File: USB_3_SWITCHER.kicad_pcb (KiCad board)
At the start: 4 copper layers, 122 x 56 mm, 218 parts, among them J1 Jack-DC, J2 Wuerth_USB3_B_Receptable_6922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, J3 Wuerth_USB3_B_Receptable_6922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, J4 Wuerth_USB3_Receptible_692122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, J5 Wuerth_USB3_Receptible_692122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, J6 Wuerth_USB3_Receptible_692122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, J7 Wuerth_USB3_Receptible_692122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, J8 Conn_01x16_Pin, J9 Conn_01x04_Pin, Q1 NTJD4401NT1G, Q2 NTJD4401NT1G, SW1 SW_Omron_B3FS, U1 AT24CS04-SSHM, U10 LM66100DCK, U11 TPD6E05U06RVZ, U12 MAX8586, U13 TPD6E05U06RVZ, U14 MAX8586, U15 TPD6E05U06RVZ, U16 MAX8586, U17 TPD6E05U06RVZ, U18 MAX8586, U19 TPD6E05U06RVZ, U2 TUSB8043A, U20 74LVC1G08, U21 74LVC1G08, U22 LM397, U3 TS3USB30EDGSR, U4 CBTL02043A, U5 LM66100DCK, U6 LMR33640ADDA, U7 LMR33640ADDA, U8 LM66100DCK, U9 TPD6E05U06RVZ, Y1 24MHz 20ppm

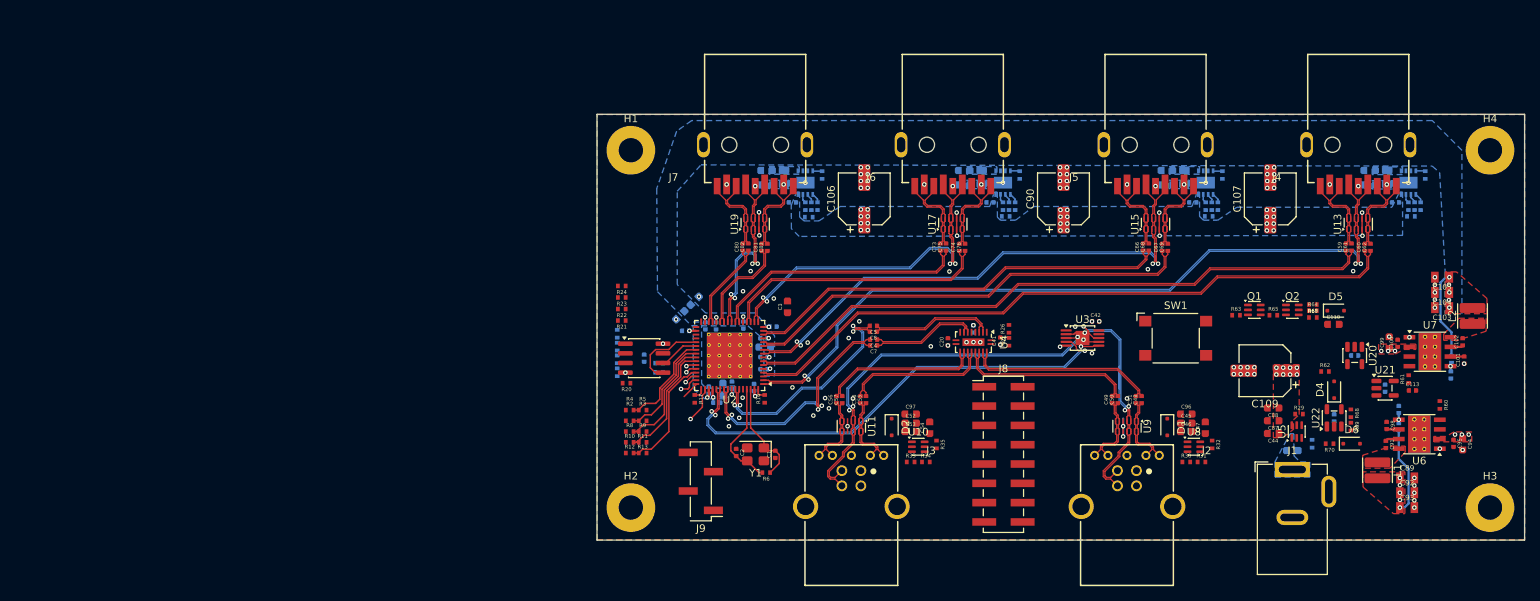
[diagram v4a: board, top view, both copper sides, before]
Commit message: Button & Power Sequencing + Layout
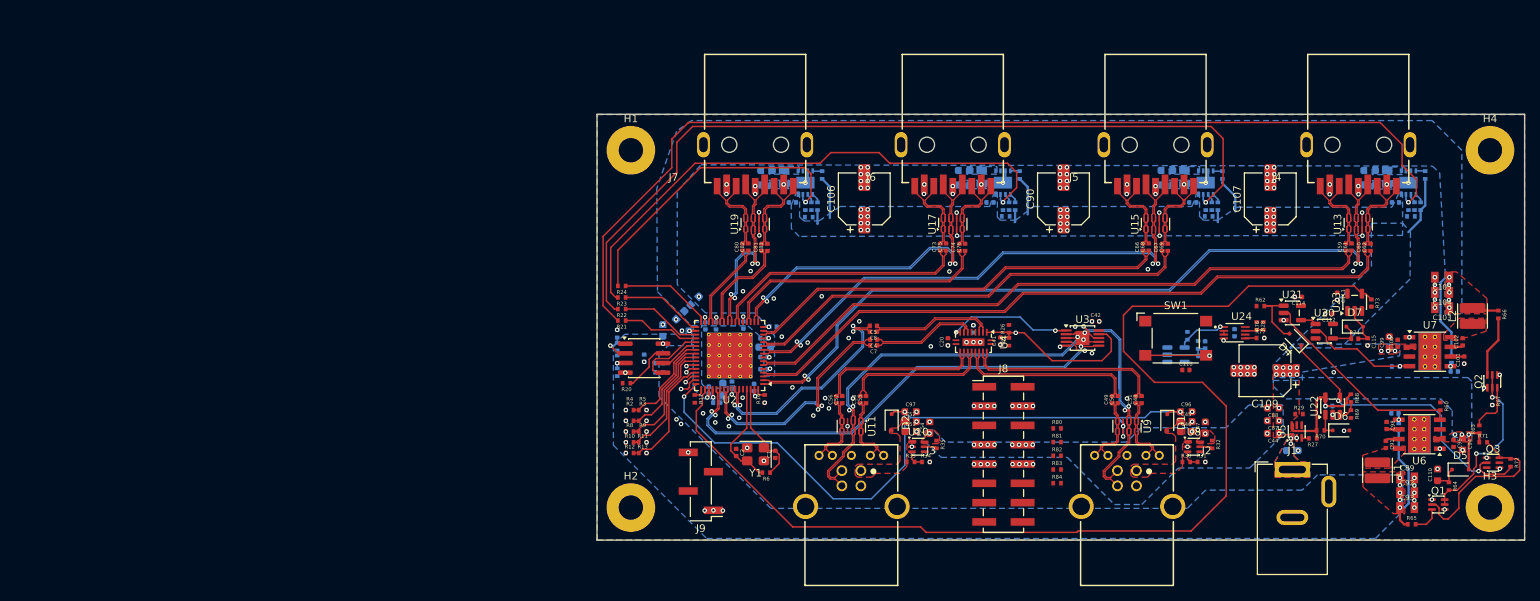
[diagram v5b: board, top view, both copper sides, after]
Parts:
- added C115: 1u, 00_Capacitor:Cap_0402, F.Cu at (242.3, 132.4)
- added C116: 100n, 00_Capacitor:Cap_0402, B.Cu at (224.8, 131.2)
- added C117: 1u, 00_Capacitor:Cap_0402, B.Cu at (221.0, 132.8)
- added C118: 100n, 00_Capacitor:Cap_0402, F.Cu at (218.4, 136.1)
- added D7: BAT54J, Diode_SMD:D_SOD-323F, F.Cu at (240.7, 130.4)
- added Q3: NTJD4401NT1G, Package_TO_SOT_SMD:SOT-363_SC-70-6, F.Cu at (258.9, 148.3)
- added R28: 10k, 00_Resistor:Res_0402, F.Cu at (227.8, 130.3)
- added R71: 1k, 00_Resistor:Res_0402, F.Cu at (257.6, 145.6)
- added R72: 0, 00_Resistor:Res_0402, F.Cu at (261.1, 148.3)
- added R73: 1K, 00_Capacitor:Cap_0402, F.Cu at (242.8, 127.3)
- added R74: 1K, 00_Capacitor:Cap_0402, F.Cu at (240.7, 132.0)
- added R75: 1K, 00_Capacitor:Cap_0402, B.Cu at (220.5, 134.3)
- added R76: 10k, 00_Resistor:Res_0402, F.Cu at (228.7, 130.3)
- added R77: 10k, 00_Resistor:Res_0402, F.Cu at (228.2, 131.9)
- added R78: 10k, 00_Resistor:Res_0402, B.Cu at (218.7, 131.6)
- added R79: 10k, 00_Resistor:Res_0402, B.Cu at (220.1, 132.8)
- added R80: 0, 00_Resistor:Res_0402, F.Cu at (201.5, 143.8)
- added R81: 0, 00_Resistor:Res_0402, F.Cu at (201.5, 145.6)
- added R82: 0, 00_Resistor:Res_0402, F.Cu at (201.5, 147.4)
- added R83: 0, 00_Resistor:Res_0402, F.Cu at (201.5, 149.2)
- added R84: 0, 00_Resistor:Res_0402, F.Cu at (201.5, 151.0)
- added U23: 74LVC1G17, Package_TO_SOT_SMD:SOT-23-5, F.Cu at (240.7, 127.2)
- added U24: 74LVC2G74, 00_IC_Package_Misc:SOP50P310X90-8N, F.Cu at (224.8, 131.2)
- added U25: 74LVC1G17, Package_TO_SOT_SMD:SOT-23-5, B.Cu at (217.2, 134.1)
- C112, C114, R27: moved to F.Cu
- C3, R61: moved to B.Cu
- R64, R70: value 10k -> 1k
- moved R63 35.3 mm to (257.1, 143.9), turned to 90 degrees
- moved Q1 35.2 mm to (251.7, 153.8)
- moved R65 33.0 mm to (248.2, 156.4)
- moved R64 29.2 mm to (253.1, 151.4), turned to -90 degrees
- moved Q2 27.9 mm to (258.8, 137.6), turned to 90 degrees
- moved D5 26.6 mm to (254.6, 149.2)
- moved R67 26.0 mm to (258.8, 140.2), turned to -90 degrees
- moved R66 24.4 mm to (259.6, 128.8), turned to -90 degrees
- moved C110 24.1 mm to (251.6, 149.9), turned to 90 degrees
- moved C3 16.7 mm to (149.7, 130.9)
- moved C113 15.9 mm to (238.3, 126.4), turned to -90 degrees
- moved U21 15.7 mm to (232.4, 128.6)
- moved C112 12.3 mm to (237.2, 128.7), turned to 180 degrees
- moved R62 12.1 mm to (228.2, 127.7)
- moved C114 10.7 mm to (233.2, 126.5)
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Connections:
- C111 pad 1: VIN -> +5V
- J8 pad 1: unconnected-(J8-Pin_1-Pad1) -> +3.3V
- J8 pad 10: unconnected-(J8-Pin_10-Pad10) -> GND
- J8 pad 2: unconnected-(J8-Pin_2-Pad2) -> +3.3V
- J8 pad 3: unconnected-(J8-Pin_3-Pad3) -> GND
- J8 pad 4: unconnected-(J8-Pin_4-Pad4) -> GND
- J8 pad 7: unconnected-(J8-Pin_7-Pad7) -> +5V
- J8 pad 8: unconnected-(J8-Pin_8-Pad8) -> +5V
- J8 pad 9: unconnected-(J8-Pin_9-Pad9) -> GND
- J9 pad 1: unconnected-(J9-Pin_1-Pad1) -> +3.3V
- J9 pad 2: unconnected-(J9-Pin_2-Pad2) -> /EXTENSION_HEADER_DEBUG/SMB_SCL
- J9 pad 3: unconnected-(J9-Pin_3-Pad3) -> /EXTENSION_HEADER_DEBUG/SMB_SDA
- J9 pad 4: unconnected-(J9-Pin_4-Pad4) -> GND
- Q1 pad 2: /POWER_SUPPLY/VIN_PGOOD -> Net-(Q1A-G)
- R63 pad 2: Net-(Q1B-D) -> Net-(Q2B-D)
- R65 pad 2: Net-(Q2B-D) -> Net-(Q1B-D)
- R68 pad 1: VIN -> +5V
- R70 pad 2: VIN -> +5V
- SW1 pad 1: unconnected-(SW1-Pad1) -> GND
- SW1 pad 2: unconnected-(SW1-Pad2) -> Net-(R75-Pad1)
- U2 pad 50: /USB_HUB/~{RESET} -> /POWER_SUPPLY/~{RESET}
- U20 pad 4: /POWER_SUPPLY/~{RESET} -> Net-(D7-K)
- U22 pad 5: VIN -> +5V
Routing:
- net /POWER_SUPPLY/~{RESET}: track 0.00 -> 151.1 mm
- net /DOWNSTREAM_CONNECTORS/VBUS_OUT_ON: track 1.17 -> 136.6 mm, vias 0 -> 1
- net /DOWNSTREAM_CONNECTORS1/VBUS_OUT_ON: track 1.17 -> 110.5 mm, vias 0 -> 1
- net VBUS: track 2.30 -> 87.6 mm, vias 0 -> 3
- net /DOWNSTREAM_CONNECTORS2/VBUS_OUT_ON: track 1.17 -> 72.6 mm, vias 0 -> 1
- net +5V: track 0.00 -> 51.6 mm, vias 38 -> 52
- net /POWER_SUPPLY/VIN_PGOOD: track 0.00 -> 40.5 mm, vias 0 -> 2
- net /DOWNSTREAM_CONNECTORS3/VBUS_OUT_ON: track 1.17 -> 40.1 mm, vias 0 -> 1
- net +3.3V: track 16.6 -> 48.2 mm, vias 12 -> 22
- net /POWER_SUPPLY/BUCK_3V3_PG: track 0.00 -> 27.8 mm
- net Net-(Q1A-G): track 0.00 -> 23.4 mm
- net Net-(Q1A-D): track 0.00 -> 22.7 mm, vias 0 -> 2
- net /HS_MUX/~{MUX_OE}: track 0.00 -> 22.6 mm, vias 0 -> 1
- net /HS_MUX/DIRECTION_SELECT: track 0.00 -> 16.6 mm, vias 0 -> 2
- net /POWER_SUPPLY/BUCK_1V1_PG: track 0.00 -> 14.5 mm, vias 0 -> 1
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- added copper zone on B.Cu, net +3.3V
- added copper zone on F.Cu, net /UPSTREAM_CON/VBUS_UPSTREAM_IN
- added copper zone on F.Cu, net /UPSTREAM_CON1/VBUS_UPSTREAM_IN
- added copper zone on F.Cu, net VIN

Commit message: Diff Pair neu, Layout fast fertig
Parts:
- removed R82, R83, R84: 0, 00_Resistor:Res_0402
- added C119: 100n, 00_Capacitor:Cap_0402, B.Cu at (193.1, 154.2)
- added C120: 100n, 00_Capacitor:Cap_0402, B.Cu at (197.2, 154.1)
- added C121: 10u, 00_Capacitor:Cap_0603, B.Cu at (197.1, 147.8)
- added C122: 10u, 00_Capacitor:Cap_0603, B.Cu at (191.9, 147.8)
- added C123: 10u, 00_Capacitor:Cap_0603, B.Cu at (154.7, 150.4)
- added C124: 10u, 00_Capacitor:Cap_0603, B.Cu at (185.9, 138.3)
- added C125: 10u, 00_Capacitor:Cap_0603, B.Cu at (201.2, 140.3)
- added C126: 10u, 00_Capacitor:Cap_0603, B.Cu at (197.6, 135.6)
- added C127: 100n, 00_Capacitor:Cap_0402, B.Cu at (189.7, 136.6)
- added C128: 100n, 00_Capacitor:Cap_0402, B.Cu at (199.0, 137.0)
- added Q4: NTJD4401NT1G, Package_TO_SOT_SMD:SOT-363_SC-70-6, B.Cu at (191.3, 151.1)
- added Q5: NTJD4401NT1G, Package_TO_SOT_SMD:SOT-363_SC-70-6, B.Cu at (187.2, 152.5)
- added R85: 10k, 00_Resistor:Res_0402, B.Cu at (197.2, 150.4)
- added R86: 10k, 00_Resistor:Res_0402, B.Cu at (195.7, 149.5)
- added R87: 10k, 00_Resistor:Res_0402, B.Cu at (191.3, 153.5)
- added R88: 10k, 00_Resistor:Res_0402, B.Cu at (187.3, 150.9)
- added R89: 10k, 00_Resistor:Res_0402, B.Cu at (201.8, 151.1)
- added R90: 10k, 00_Resistor:Res_0402, B.Cu at (197.2, 152.3)
- added R91: 10k, 00_Resistor:Res_0402, B.Cu at (199.8, 149.6)
- added R92: 10k, 00_Resistor:Res_0402, B.Cu at (189.4, 153.9)
- added U26: 74LVC1G32, Package_TO_SOT_SMD:SOT-23-5, B.Cu at (195.1, 152.3)
- added U27: 74LVC1G08, Package_TO_SOT_SMD:SOT-23-5, B.Cu at (199.2, 152.3)
- added U28: ISO1540, Package_SO:SOIC-8_3.9x4.9mm_P1.27mm, B.Cu at (194.3, 138.9)
- H1, H2, H3, H4: value MountingHole_Pad_MP -> MountingHole_Pad; footprint MountingHole:MountingHole_3.2mm_M3_Pad -> MountingHole:MountingHole_3.2mm_M3_Pad_TopBottom
- R80, R81: footprint 00_Resistor:Res_0402 -> 00_Resistor:Res_0603; moved to B.Cu
- U11, U9: moved to B.Cu
- moved R80 14.0 mm to (188.7, 138.3), turned to 180 degrees
- moved R81 7.36 mm to (200.3, 138.3)
- moved C48 0.50 mm to (212.6, 139.5)
- moved C49 0.50 mm to (208.8, 139.5)
- moved C50 0.50 mm to (209.5, 139.5)
- moved C51 0.50 mm to (211.9, 139.5)
- moved C55 0.50 mm to (176.4, 139.5)
- moved C56 0.50 mm to (172.5, 139.5)
- moved C57 0.50 mm to (173.2, 139.5)
- moved C58 0.50 mm to (175.7, 139.5)
- moved R46 0.49 mm to (195.2, 115.9)
- moved C77 0.41 mm to (193.1, 114.0)
- moved C78 0.41 mm to (189.7, 109.8)
- moved C79 0.41 mm to (189.7, 111.7)
- moved FB3 0.41 mm to (192.0, 110.7)
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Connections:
- H1 pad 1: (no net) -> GND
- H2 pad 1: (no net) -> GND
- H3 pad 1: (no net) -> GND
- H4 pad 1: (no net) -> GND
- J8 pad 1: +3.3V -> Net-(J8-Pin_1)
- J8 pad 11: unconnected-(J8-Pin_11-Pad11) -> Net-(J8-Pin_11)
- J8 pad 12: unconnected-(J8-Pin_12-Pad12) -> VCC_EXT
- J8 pad 13: unconnected-(J8-Pin_13-Pad13) -> /EXTENSION_HEADER_DEBUG/DIRECTION_EXT
- J8 pad 14: unconnected-(J8-Pin_14-Pad14) -> /EXTENSION_HEADER_DEBUG/~{MUX_OE_EXT}
- J8 pad 16: unconnected-(J8-Pin_16-Pad16) -> GND
- J8 pad 2: +3.3V -> Net-(J8-Pin_2)
- J8 pad 5: unconnected-(J8-Pin_5-Pad5) -> /EXTENSION_HEADER_DEBUG/I2C_SDA_EXT
- J8 pad 6: unconnected-(J8-Pin_6-Pad6) -> /EXTENSION_HEADER_DEBUG/I2C_SCL_EXT
- J9 pad 2: /EXTENSION_HEADER_DEBUG/SMB_SCL -> /USB_HUB/SMB_SCL
- J9 pad 3: /EXTENSION_HEADER_DEBUG/SMB_SDA -> /USB_HUB/SMB_SDA
- R73 pad 1: /POWER_SUPPLY/~{RESET} -> /DIRECTION_SWITCH/~{RESET}
- R80 pad 1: unconnected-(R80-Pad1) -> Net-(J8-Pin_1)
- R80 pad 2: Net-(R80-Pad2) -> +3.3V
- R81 pad 1: Net-(R80-Pad2) -> Net-(J8-Pin_2)
- R81 pad 2: /EXTENSION_HEADER_DEBUG/DIRECTION -> +3.3V
- U2 pad 50: /POWER_SUPPLY/~{RESET} -> /DIRECTION_SWITCH/~{RESET}
- U23 pad 4: /POWER_SUPPLY/~{RESET} -> /DIRECTION_SWITCH/~{RESET}
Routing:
- net /DIRECTION_SWITCH/~{RESET}: track 0.00 -> 167.4 mm, vias 0 -> 2
- net /POWER_SUPPLY/~{RESET}: track 151.1 -> 0.00 mm
- net /DOWNSTREAM_CONNECTORS/~{USB_DS_OC}: track 1.67 -> 149.6 mm, vias 1 -> 3
- net /DOWNSTREAM_CONNECTORS1/~{USB_DS_OC}: track 2.75 -> 113.0 mm, vias 1 -> 3
- net /DOWNSTREAM_CONNECTORS2/~{USB_DS_OC}: track 1.45 -> 79.6 mm, vias 1 -> 3
- net /DOWNSTREAM_CONNECTORS3/~{USB_DS_OC}: track 1.32 -> 43.0 mm, vias 1 -> 3
- net VBUS: track 87.6 -> 51.4 mm
- net /USB_HUB/SMB_SCL: track 5.26 -> 36.4 mm, vias 0 -> 2
- net GND: track 19.8 -> 48.7 mm, vias 177 -> 197
- net VCC_EXT: track 0.00 -> 28.8 mm, vias 0 -> 2
- net /USB_HUB/SMB_SDA: track 9.32 -> 37.9 mm, vias 0 -> 1
- net +3.3V: track 48.2 -> 75.7 mm, vias 22 -> 32
- net /DIRECTION_SWITCH/DIRECTION: track 1.51 -> 23.3 mm, vias 0 -> 1
- net Net-(Q4B-D): track 0.00 -> 11.4 mm
- net /EXTENSION_HEADER_DEBUG/~{MUX_OE_EXT}: track 0.00 -> 10.0 mm, vias 0 -> 1
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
